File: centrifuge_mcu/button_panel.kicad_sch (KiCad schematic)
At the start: 0 parts

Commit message: make and pick footprints for almost everything
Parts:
- added R127, R128, R129, R130: 10k, symbol Device:R
- added U106: 4x4_keyboard, centrifuge_mcu:Adafruit 3844, symbol mcu_centrifuge_library:4x4_keyboard
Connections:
- new net: R128.1, U106.5 (R0)
- new net: R130.1, U106.6 (R1)
- new net: R127.1, U106.7 (R2)
- new net: R129.1, U106.8 (R3)
- new net C0: U106.1 (C0)
- new net C1: U106.2 (C1)
- new net C2: U106.3 (C2)
- new net C3: U106.4 (C3)
- new net R0: R128.2
- new net R1: R130.2
- new net R2: R127.2
- new net R3: R129.2
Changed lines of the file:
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@@
 (kicad_sch (version 20211123) (generator eeschema)
   (paper "A4")
+  (wire (pts (xy 170.18 125.73) (xy 180.975 125.73))
+    (stroke (width 0) (type default) (color 0 0 0 0))
+  )
+  (wire (pts (xy 177.8 114.3) (xy 180.975 114.3))
+    (stroke (width 0) (type default) (color 0 0 0 0))
+  )
+  (wire (pts (xy 144.78 114.3) (xy 144.78 101.6))
+    (stroke (width 0) (type default) (color 0 0 0 0))
+  )
+  (wire (pts (xy 162.56 125.73) (xy 154.94 125.73))
+    (stroke (width 0) (type default) (color 0 0 0 0))
+  )
+  (wire (pts (xy 170.18 121.92) (xy 157.48 121.92))
+    (stroke (width 0) (type default) (color 0 0 0 0))
+  )
+  (wire (pts (xy 170.18 118.11) (xy 180.975 118.11))
+    (stroke (width 0) (type default) (color 0 0 0 0))
+  )
+  (wire (pts (xy 162.56 114.3) (xy 162.56 101.6))
+    (stroke (width 0) (type default) (color 0 0 0 0))
+  )
+  (wire (pts (xy 162.56 118.11) (xy 160.02 118.11))
+    (stroke (width 0) (type default) (color 0 0 0 0))
+  )
+  (wire (pts (xy 125.73 121.92) (xy 149.86 121.92))
+    (stroke (width 0) (type default) (color 0 0 0 0))
+  )
+  (wire (pts (xy 177.8 121.92) (xy 180.975 121.92))
+    (stroke (width 0) (type default) (color 0 0 0 0))
+  )
+  (wire (pts (xy 152.4 125.73) (xy 152.4 101.6))
+    (stroke (width 0) (type default) (color 0 0 0 0))
+  )
+  (wire (pts (xy 125.73 125.73) (xy 152.4 125.73))
+    (stroke (width 0) (type default) (color 0 0 0 0))
+  )
+  (wire (pts (xy 157.48 121.92) (xy 157.48 101.6))
+    (stroke (width 0) (type default) (color 0 0 0 0))
+  )
+  (wire (pts (xy 170.18 114.3) (xy 162.56 114.3))
+    (stroke (width 0) (type default) (color 0 0 0 0))
+  )
+  (wire (pts (xy 125.73 118.11) (xy 147.32 118.11))
+    (stroke (width 0) (type default) (color 0 0 0 0))
+  )
+  (wire (pts (xy 147.32 118.11) (xy 147.32 101.6))
+    (stroke (width 0) (type default) (color 0 0 0 0))
+  )
+  (wire (pts (xy 160.02 118.11) (xy 160.02 101.6))
+    (stroke (width 0) (type default) (color 0 0 0 0))
+  )
+  (wire (pts (xy 154.94 125.73) (xy 154.94 101.6))
+    (stroke (width 0) (type default) (color 0 0 0 0))
+  )
+  (wire (pts (xy 149.86 121.92) (xy 149.86 101.6))
+    (stroke (width 0) (type default) (color 0 0 0 0))
+  )
+  (wire (pts (xy 125.73 114.3) (xy 144.78 114.3))
+    (stroke (width 0) (type default) (color 0 0 0 0))
+  )
+  (hierarchical_label "C1" (shape output) (at 125.73 118.11 180)
+    (effects (font (size 1.27 1.27)) (justify right))
+  )
+  (hierarchical_label "R0" (shape input) (at 180.975 125.73 0)
+    (effects (font (size 1.27 1.27)) (justify left))
+  )
+  (hierarchical_label "R3" (shape input) (at 180.975 114.3 0)
+    (effects (font (size 1.27 1.27)) (justify left))
+  )
+  (hierarchical_label "C2" (shape output) (at 125.73 121.92 180)
+    (effects (font (size 1.27 1.27)) (justify right))
+  )
+  (hierarchical_label "C0" (shape output) (at 125.73 114.3 180)
+    (effects (font (size 1.27 1.27)) (justify right))
+  )
+  (hierarchical_label "C3" (shape output) (at 125.73 125.73 180)
+    (effects (font (size 1.27 1.27)) (justify right))
+  )
+  (hierarchical_label "R2" (shape input) (at 180.975 118.11 0)
+    (effects (font (size 1.27 1.27)) (justify left))
+  )
+  (hierarchical_label "R1" (shape input) (at 180.975 121.92 0)
+    (effects (font (size 1.27 1.27)) (justify left))
+  )
+  (symbol (lib_id "mcu_centrifuge_library:4x4_keyboard") (at 153.67 91.44 0) (unit 1)
+    (in_bom yes) (on_board yes) (fields_autoplaced)
+    (property "Reference" "U106" (id 0) (at 167.64 83.1849 0)
+      (effects (font (size 1.27 1.27)) (justify left))
+    )
+    (property "Value" "4x4_keyboard" (id 1) (at 167.64 85.7249 0)
+      (effects (font (size 1.27 1.27)) (justify left))
+    )
+    (property "Footprint" "centrifuge_mcu:Adafruit 3844" (id 2) (at 153.67 91.44 0)
+      (effects (font (size 1.27 1.27)) hide)
+    )
+    (property "Datasheet" "https://no.mouser.com/ProductDetail/Adafruit/3844?qs=qSfuJ%252Bfl%2Fd6WS5%252BJGim1hw%3D%3D" (id 3) (at 153.67 68.58 0)
+      (effects (font (size 1.27 1.27)) hide)
+    )
+    (pin "1")
+    (pin "2")
+    (pin "3")
+    (pin "4")
+    (pin "5")
+    (pin "6")
+    (pin "7")
+    (pin "8")
+  )
+  (symbol (lib_id "Device:R") (at 166.37 118.11 90) (unit 1)
+    (in_bom yes) (on_board yes)
+    (property "Reference" "R127" (id 0) (at 166.37 115.57 90))
+    (property "Value" "10k" (id 1) (at 166.37 118.11 90))
+    (property "Footprint" "" (id 2) (at 166.37 119.888 90)
+      (effects (font (size 1.27 1.27)) hide)
+    )
+    (property "Datasheet" "~" (id 3) (at 166.37 118.11 0)
+      (effects (font (size 1.27 1.27)) hide)
+    )
+    (pin "1")
+    (pin "2")
+  )
+  (symbol (lib_id "Device:R") (at 173.99 114.3 90) (unit 1)
+    (in_bom yes) (on_board yes)
+    (property "Reference" "R129" (id 0) (at 173.99 111.76 90))
+    (property "Value" "10k" (id 1) (at 173.99 114.3 90))
+    (property "Footprint" "" (id 2) (at 173.99 116.078 90)
+      (effects (font (size 1.27 1.27)) hide)
+    )
+    (property "Datasheet" "~" (id 3) (at 173.99 114.3 0)
+      (effects (font (size 1.27 1.27)) hide)
+    )
+    (pin "1")
+    (pin "2")
+  )
+  (symbol (lib_id "Device:R") (at 173.99 121.92 90) (unit 1)
+    (in_bom yes) (on_board yes)
+    (property "Reference" "R130" (id 0) (at 173.99 119.38 90))
+    (property "Value" "10k" (id 1) (at 173.99 121.92 90))
+    (property "Footprint" "" (id 2) (at 173.99 123.698 90)
+      (effects (font (size 1.27 1.27)) hide)
+    )
+    (property "Datasheet" "~" (id 3) (at 173.99 121.92 0)
+      (effects (font (size 1.27 1.27)) hide)
+    )
+    (pin "1")
+    (pin "2")
+  )
+  (symbol (lib_id "Device:R") (at 166.37 125.73 90) (unit 1)
+    (in_bom yes) (on_board yes)
+    (property "Reference" "R128" (id 0) (at 166.37 123.19 90))
+    (property "Value" "10k" (id 1) (at 166.37 125.73 90))
+    (property "Footprint" "" (id 2) (at 166.37 127.508 90)
+      (effects (font (size 1.27 1.27)) hide)
+    )
+    (property "Datasheet" "~" (id 3) (at 166.37 125.73 0)
+      (effects (font (size 1.27 1.27)) hide)
+    )
+    (pin "1")
+    (pin "2")
+  )
 )

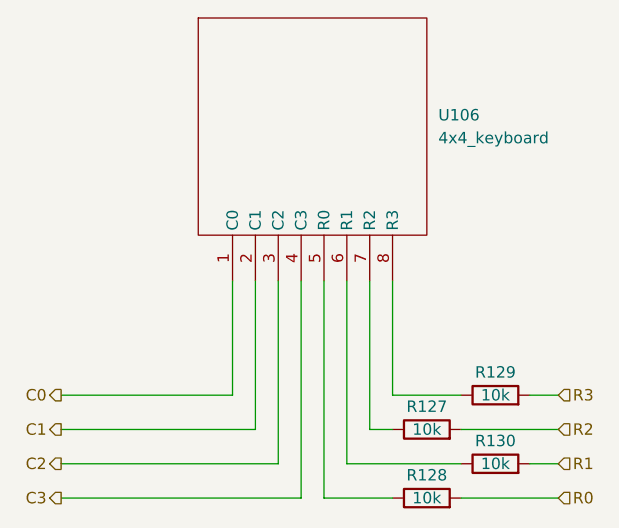
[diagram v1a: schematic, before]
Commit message: more footprints, add links to resistor and inductance purchase
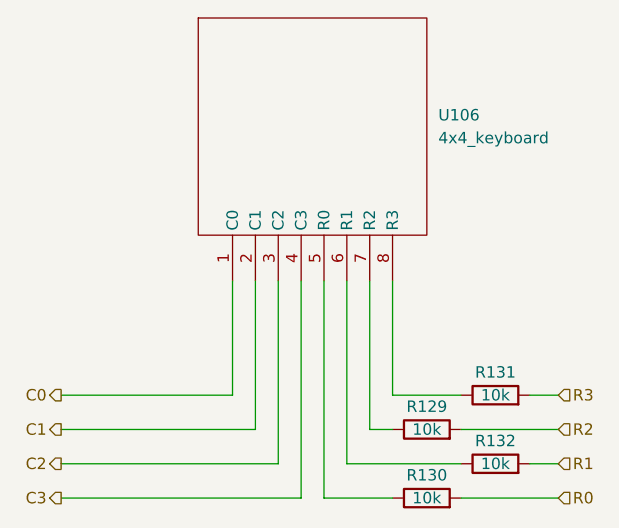
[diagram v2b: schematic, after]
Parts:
- R129: renamed from R127; footprint (none) -> Resistor_SMD:R_0805_2012Metric_Pad1.20x1.40mm_HandSolder; Purchase (none) -> https://www.digikey.no/no/products/detail/yageo/AC0805FR-07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
- R130: renamed from R128; footprint (none) -> Resistor_SMD:R_0805_2012Metric_Pad1.20x1.40mm_HandSolder; Purchase (none) -> https://www.digikey.no/no/products/detail/yageo/AC0805FR-07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
- R131: renamed from R129; footprint (none) -> Resistor_SMD:R_0805_2012Metric_Pad1.20x1.40mm_HandSolder; Purchase (none) -> https://www.digikey.no/no/products/detail/yageo/AC0805FR-07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
- R132: renamed from R130; footprint (none) -> Resistor_SMD:R_0805_2012Metric_Pad1.20x1.40mm_HandSolder; Purchase (none) -> https://www.digikey.no/no/products/detail/yageo/AC0805FR-07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
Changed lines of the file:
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@@
   (symbol (lib_id "Device:R") (at 166.37 118.11 90) (unit 1)
     (in_bom yes) (on_board yes)
-    (property "Reference" "R127" (id 0) (at 166.37 115.57 90))
+    (property "Reference" "R129" (id 0) (at 166.37 115.57 90))
     (property "Value" "10k" (id 1) (at 166.37 118.11 90))
-    (property "Footprint" "" (id 2) (at 166.37 119.888 90)
+    (property "Footprint" "Resistor_SMD:R_0805_2012Metric_Pad1.20x1.40mm_HandSolder" (id 2) (at 166.37 119.888 90)
       (effects (font (size 1.27 1.27)) hide)
     )
     (property "Datasheet" "~" (id 3) (at 166.37 118.11 0)
+      (effects (font (size 1.27 1.27)) hide)
+    )
+    (property "Purchase" "https://www.digikey.no/no/products/detail/yageo/AC0805FR-0710KL/2827834" (id 4) (at 166.37 118.11 0)
       (effects (font (size 1.27 1.27)) hide)
     )
@@
   (symbol (lib_id "Device:R") (at 173.99 114.3 90) (unit 1)
     (in_bom yes) (on_board yes)
-    (property "Reference" "R129" (id 0) (at 173.99 111.76 90))
+    (property "Reference" "R131" (id 0) (at 173.99 111.76 90))
     (property "Value" "10k" (id 1) (at 173.99 114.3 90))
-    (property "Footprint" "" (id 2) (at 173.99 116.078 90)
+    (property "Footprint" "Resistor_SMD:R_0805_2012Metric_Pad1.20x1.40mm_HandSolder" (id 2) (at 173.99 116.078 90)
       (effects (font (size 1.27 1.27)) hide)
     )
     (property "Datasheet" "~" (id 3) (at 173.99 114.3 0)
+      (effects (font (size 1.27 1.27)) hide)
+    )
+    (property "Purchase" "https://www.digikey.no/no/products/detail/yageo/AC0805FR-0710KL/2827834" (id 4) (at 173.99 114.3 0)
       (effects (font (size 1.27 1.27)) hide)
     )
@@
   (symbol (lib_id "Device:R") (at 173.99 121.92 90) (unit 1)
     (in_bom yes) (on_board yes)
-    (property "Reference" "R130" (id 0) (at 173.99 119.38 90))
+    (property "Reference" "R132" (id 0) (at 173.99 119.38 90))
     (property "Value" "10k" (id 1) (at 173.99 121.92 90))
-    (property "Footprint" "" (id 2) (at 173.99 123.698 90)
+    (property "Footprint" "Resistor_SMD:R_0805_2012Metric_Pad1.20x1.40mm_HandSolder" (id 2) (at 173.99 123.698 90)
       (effects (font (size 1.27 1.27)) hide)
     )
     (property "Datasheet" "~" (id 3) (at 173.99 121.92 0)
+      (effects (font (size 1.27 1.27)) hide)
+    )
+    (property "Purchase" "https://www.digikey.no/no/products/detail/yageo/AC0805FR-0710KL/2827834" (id 4) (at 173.99 121.92 0)
       (effects (font (size 1.27 1.27)) hide)
     )
@@
   (symbol (lib_id "Device:R") (at 166.37 125.73 90) (unit 1)
     (in_bom yes) (on_board yes)
-    (property "Reference" "R128" (id 0) (at 166.37 123.19 90))
+    (property "Reference" "R130" (id 0) (at 166.37 123.19 90))
     (property "Value" "10k" (id 1) (at 166.37 125.73 90))
-    (property "Footprint" "" (id 2) (at 166.37 127.508 90)
+    (property "Footprint" "Resistor_SMD:R_0805_2012Metric_Pad1.20x1.40mm_HandSolder" (id 2) (at 166.37 127.508 90)
       (effects (font (size 1.27 1.27)) hide)
     )
@@
       (effects (font (size 1.27 1.27)) hide)
     )
+    (property "Purchase" "https://www.digikey.no/no/products/detail/yageo/AC0805FR-0710KL/2827834" (id 4) (at 166.37 125.73 0)
+      (effects (font (size 1.27 1.27)) hide)
+    )

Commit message: last footprints, time to route (after final FPGA-board connectors)
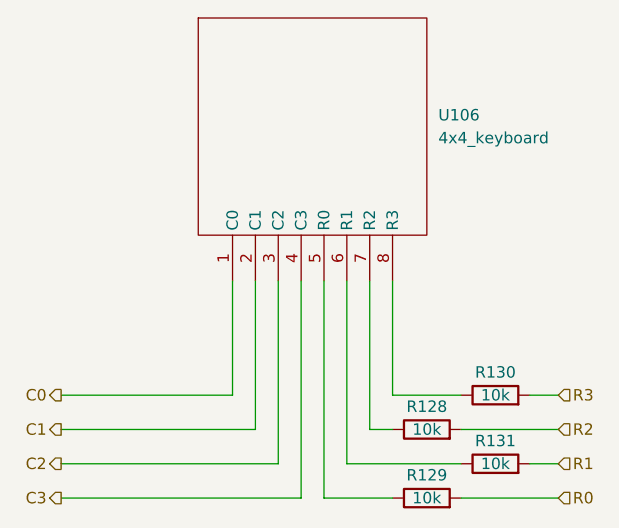
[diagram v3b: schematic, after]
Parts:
- renumbered R129 to R128, R130 to R129, R131 to R130, R132 to R131
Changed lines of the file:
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@@
   (symbol (lib_id "Device:R") (at 166.37 118.11 90) (unit 1)
     (in_bom yes) (on_board yes)
-    (property "Reference" "R129" (id 0) (at 166.37 115.57 90))
+    (property "Reference" "R128" (id 0) (at 166.37 115.57 90))
     (property "Value" "10k" (id 1) (at 166.37 118.11 90))
     (property "Footprint" "Resistor_SMD:R_0805_2012Metric_Pad1.20x1.40mm_HandSolder" (id 2) (at 166.37 119.888 90)
@@
   (symbol (lib_id "Device:R") (at 173.99 114.3 90) (unit 1)
     (in_bom yes) (on_board yes)
-    (property "Reference" "R131" (id 0) (at 173.99 111.76 90))
+    (property "Reference" "R130" (id 0) (at 173.99 111.76 90))
     (property "Value" "10k" (id 1) (at 173.99 114.3 90))
     (property "Footprint" "Resistor_SMD:R_0805_2012Metric_Pad1.20x1.40mm_HandSolder" (id 2) (at 173.99 116.078 90)
@@
   (symbol (lib_id "Device:R") (at 173.99 121.92 90) (unit 1)
     (in_bom yes) (on_board yes)
-    (property "Reference" "R132" (id 0) (at 173.99 119.38 90))
+    (property "Reference" "R131" (id 0) (at 173.99 119.38 90))
     (property "Value" "10k" (id 1) (at 173.99 121.92 90))
     (property "Footprint" "Resistor_SMD:R_0805_2012Metric_Pad1.20x1.40mm_HandSolder" (id 2) (at 173.99 123.698 90)
@@
   (symbol (lib_id "Device:R") (at 166.37 125.73 90) (unit 1)
     (in_bom yes) (on_board yes)
-    (property "Reference" "R130" (id 0) (at 166.37 123.19 90))
+    (property "Reference" "R129" (id 0) (at 166.37 123.19 90))
     (property "Value" "10k" (id 1) (at 166.37 125.73 90))
     (property "Footprint" "Resistor_SMD:R_0805_2012Metric_Pad1.20x1.40mm_HandSolder" (id 2) (at 166.37 127.508 90)

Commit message: start routing PCB for the MCU, starting with power
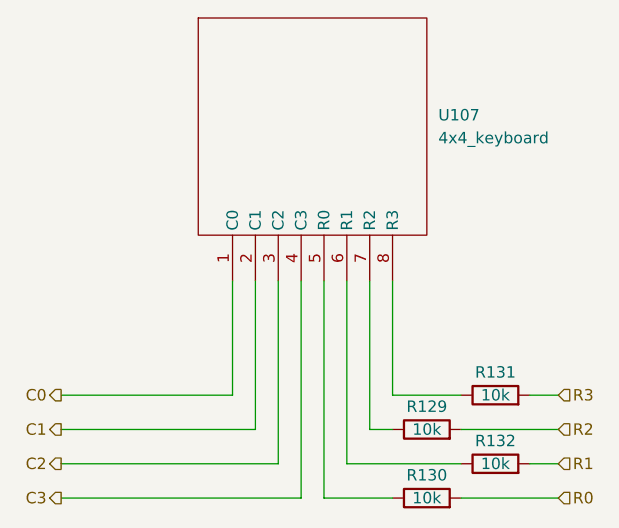
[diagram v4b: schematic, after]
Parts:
- renumbered R128 to R129, R129 to R130, R130 to R131, R131 to R132, U106 to U107
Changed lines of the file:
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@@
   (symbol (lib_id "mcu_centrifuge_library:4x4_keyboard") (at 153.67 91.44 0) (unit 1)
     (in_bom yes) (on_board yes) (fields_autoplaced)
-    (property "Reference" "U106" (id 0) (at 167.64 83.1849 0)
+    (property "Reference" "U107" (id 0) (at 167.64 83.1849 0)
       (effects (font (size 1.27 1.27)) (justify left))
     )
@@
   (symbol (lib_id "Device:R") (at 166.37 118.11 90) (unit 1)
     (in_bom yes) (on_board yes)
-    (property "Reference" "R128" (id 0) (at 166.37 115.57 90))
+    (property "Reference" "R129" (id 0) (at 166.37 115.57 90))
     (property "Value" "10k" (id 1) (at 166.37 118.11 90))
     (property "Footprint" "Resistor_SMD:R_0805_2012Metric_Pad1.20x1.40mm_HandSolder" (id 2) (at 166.37 119.888 90)
@@
   (symbol (lib_id "Device:R") (at 173.99 114.3 90) (unit 1)
     (in_bom yes) (on_board yes)
-    (property "Reference" "R130" (id 0) (at 173.99 111.76 90))
+    (property "Reference" "R131" (id 0) (at 173.99 111.76 90))
     (property "Value" "10k" (id 1) (at 173.99 114.3 90))
     (property "Footprint" "Resistor_SMD:R_0805_2012Metric_Pad1.20x1.40mm_HandSolder" (id 2) (at 173.99 116.078 90)
@@
   (symbol (lib_id "Device:R") (at 173.99 121.92 90) (unit 1)
     (in_bom yes) (on_board yes)
-    (property "Reference" "R131" (id 0) (at 173.99 119.38 90))
+    (property "Reference" "R132" (id 0) (at 173.99 119.38 90))
     (property "Value" "10k" (id 1) (at 173.99 121.92 90))
     (property "Footprint" "Resistor_SMD:R_0805_2012Metric_Pad1.20x1.40mm_HandSolder" (id 2) (at 173.99 123.698 90)
@@
   (symbol (lib_id "Device:R") (at 166.37 125.73 90) (unit 1)
     (in_bom yes) (on_board yes)
-    (property "Reference" "R129" (id 0) (at 166.37 123.19 90))
+    (property "Reference" "R130" (id 0) (at 166.37 123.19 90))
     (property "Value" "10k" (id 1) (at 166.37 125.73 90))
     (property "Footprint" "Resistor_SMD:R_0805_2012Metric_Pad1.20x1.40mm_HandSolder" (id 2) (at 166.37 127.508 90)
